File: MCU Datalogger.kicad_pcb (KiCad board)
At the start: 2 copper layers, 51.4 x 34.3 mm, 31 parts, among them J1 Conn_01x04_Male, J2 Conn_01x09_Male, J3 Conn_01x04_Male, J4 Conn_02x03_Odd_Even, U1 24LC1025, U2 DS1337S+, U3 24LC1025, U4 ATMEGA328P-AU, Y1 32.768 KHz, Y2 16 MHz

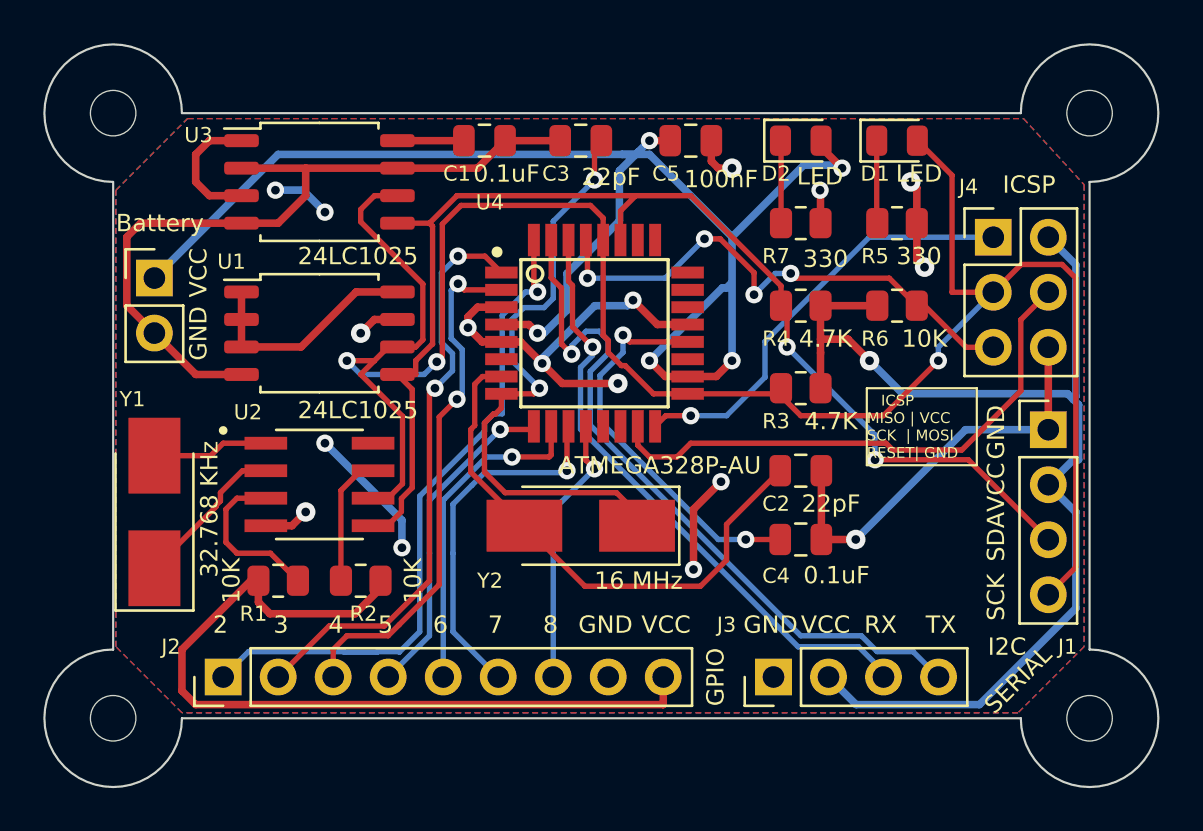
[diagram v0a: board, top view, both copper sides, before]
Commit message: Completed 4-layer pcb routing.
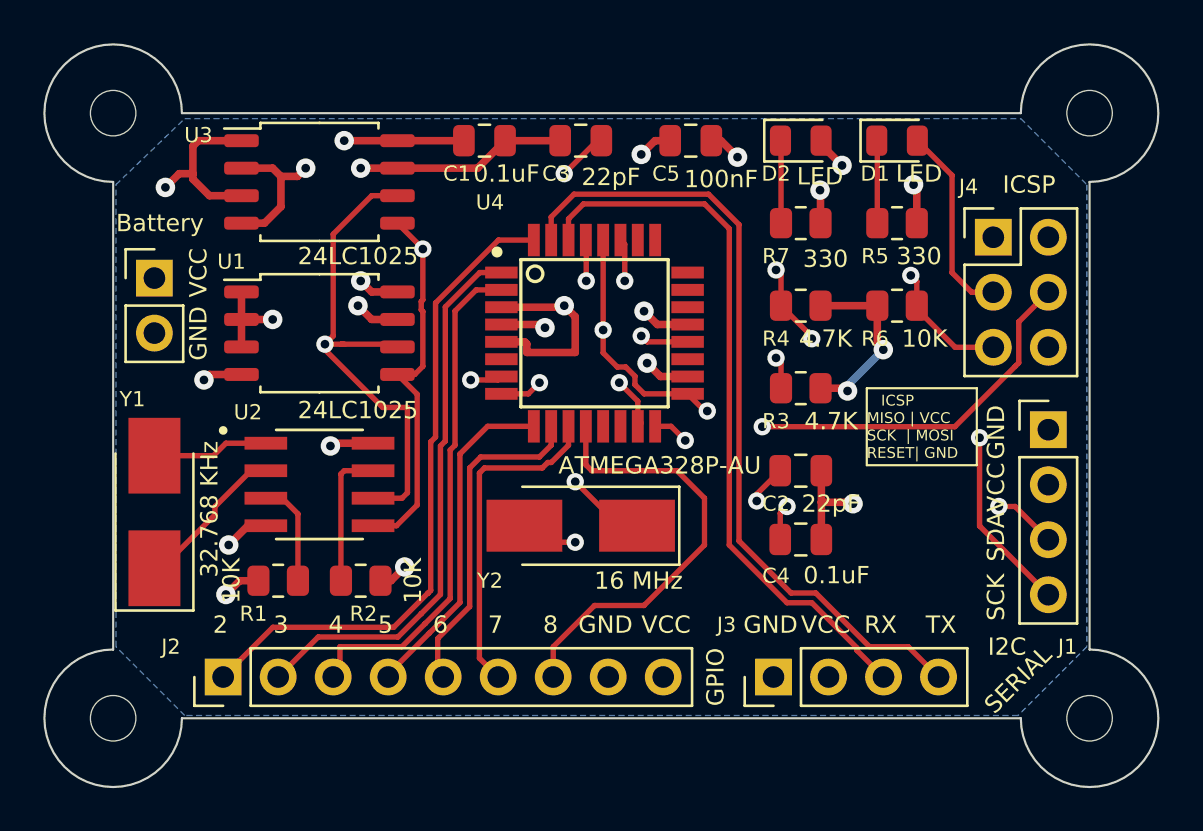
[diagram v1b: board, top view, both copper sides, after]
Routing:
- net /Vcc: track 188.4 -> 45.9 mm, vias 10 -> 13
- net GND: track 90.4 -> 43.5 mm, vias 13 -> 11
- net /D8: track 12.5 -> 20.4 mm, vias 1 -> 0
- net /SCK: track 98.0 -> 90.8 mm, vias 3 -> 5
- net /RX: track 28.3 -> 33.5 mm, vias 1 -> 0
- net Net-(Y2-Pad1): track 28.8 -> 24.8 mm, vias 2 -> 3
- net /TX: track 33.3 -> 37.2 mm, vias 1 -> 0
- net Net-(U2-Pad3): track 7.64 -> 4.87 mm
- net /SDA: track 58.3 -> 56.4 mm, vias 2 -> 5
- net /D7: track 16.9 -> 15.3 mm, vias 1 -> 0
- net /D3: track 27.2 -> 25.7 mm, vias 2 -> 0
- net /MOSI: track 25.4 -> 26.9 mm, vias 0 -> 2
- net /RESET: track 24.8 -> 23.7 mm, vias 4 -> 2
- net Net-(U4-Pad20): track 18.1 -> 18.9 mm
- net /D4: track 24.2 -> 23.5 mm, vias 2 -> 0
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- added copper zone on In2.Cu, net /Vcc
- removed copper zone on F.Cu, net /Vcc
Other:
- copper layers 2 -> 4

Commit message: Added board characteristics.
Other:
- board text added: "4.6900 mm"
- board text removed: "1.6000 mm"
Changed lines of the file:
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@@
       (plotinvisibletext false)
       (sketchpadsonfab false)
-      (subtractmaskfromsilk false)
+      (subtractmaskfromsilk true)
       (outputformat 1)
       (mirror false)
       (drillshape 0)
       (scaleselection 1)
-      (outputdirectory "MCU_Datalogger_Gerbers/")
+      (outputdirectory "4_layer_MCU_Datalogger_Gerbers")
     )
   )
@@
     (effects (font (size 0.8 0.8) (thickness 0.15)))
   )
-  (gr_text "Castellated pads: " (at 144.641 99.287) (layer "User.1")
+  (gr_text "Min track/spacing: " (at 146.8 90.13) (layer "User.1")
     (effects (font (size 1.5 1.5) (thickness 0.2)) (justify left top))
   )
-  (gr_text "No" (at 236.098143 99.287) (layer "User.1")
+  (gr_text "4.6900 mm" (at 238.257143 81.1) (layer "User.1")
     (effects (font (size 1.5 1.5) (thickness 0.2)) (justify left top))
   )
-  (gr_text "None" (at 177.198143 94.772) (layer "User.1")
+  (gr_text "Impedance Control: " (at 213.414286 94.645) (layer "User.1")
     (effects (font (size 1.5 1.5) (thickness 0.2)) (justify left top))
   )
-  (gr_text "1.6000 mm" (at 236.098143 81.227) (layer "User.1")
+  (gr_text "Board overall dimensions: " (at 146.8 85.615) (layer "User.1")
     (effects (font (size 1.5 1.5) (thickness 0.2)) (justify left top))
   )
-  (gr_text "" (at 211.255286 85.742) (layer "User.1")
+  (gr_text "0.2000 mm / 0.0000 mm" (at 179.357143 90.13) (layer "User.1")
     (effects (font (size 1.5 1.5) (thickness 0.2)) (justify left top))
   )
-  (gr_text "51.7350 mm x 34.5900 mm" (at 177.198143 85.742) (layer "User.1")
+  (gr_text "" (at 238.257143 85.615) (layer "User.1")
     (effects (font (size 1.5 1.5) (thickness 0.2)) (justify left top))
   )
-  (gr_text "0.2000 mm / 0.0000 mm" (at 177.198143 90.257) (layer "User.1")
+  (gr_text "51.7350 mm x 34.5900 mm" (at 179.357143 85.615) (layer "User.1")
     (effects (font (size 1.5 1.5) (thickness 0.2)) (justify left top))
   )
-  (gr_text "Min track/spacing: " (at 144.641 90.257) (layer "User.1")
+  (gr_text "Copper Layer Count: " (at 146.8 81.1) (layer "User.1")
     (effects (font (size 1.5 1.5) (thickness 0.2)) (justify left top))
   )
-  (gr_text "Min hole diameter: " (at 211.255286 90.257) (layer "User.1")
+  (gr_text "4" (at 179.357143 81.1) (layer "User.1")
     (effects (font (size 1.5 1.5) (thickness 0.2)) (justify left top))
   )
-  (gr_text "Board overall dimensions: " (at 144.641 85.742) (layer "User.1")
+  (gr_text "No" (at 238.257143 99.16) (layer "User.1")
     (effects (font (size 1.5 1.5) (thickness 0.2)) (justify left top))
   )
-  (gr_text "0.3000 mm" (at 236.098143 90.257) (layer "User.1")
+  (gr_text "Castellated pads: " (at 146.8 99.16) (layer "User.1")
     (effects (font (size 1.5 1.5) (thickness 0.2)) (justify left top))
   )
-  (gr_text "2" (at 177.198143 81.227) (layer "User.1")
+  (gr_text "Copper Finish: " (at 146.8 94.645) (layer "User.1")
     (effects (font (size 1.5 1.5) (thickness 0.2)) (justify left top))
   )
-  (gr_text "" (at 236.098143 85.742) (layer "User.1")
+  (gr_text "" (at 213.414286 85.615) (layer "User.1")
     (effects (font (size 1.5 1.5) (thickness 0.2)) (justify left top))
   )
-  (gr_text "Board Thickness: " (at 211.255286 81.227) (layer "User.1")
+  (gr_text "None" (at 179.357143 94.645) (layer "User.1")
     (effects (font (size 1.5 1.5) (thickness 0.2)) (justify left top))
   )
-  (gr_text "No" (at 236.098143 94.772) (layer "User.1")
+  (gr_text "Board Thickness: " (at 213.414286 81.1) (layer "User.1")
     (effects (font (size 1.5 1.5) (thickness 0.2)) (justify left top))
   )
-  (gr_text "Copper Layer Count: " (at 144.641 81.227) (layer "User.1")
+  (gr_text "No" (at 179.357143 99.16) (layer "User.1")
     (effects (font (size 1.5 1.5) (thickness 0.2)) (justify left top))
   )
-  (gr_text "Plated Board Edge: " (at 211.255286 99.287) (layer "User.1")
+  (gr_text "Min hole diameter: " (at 213.414286 90.13) (layer "User.1")
     (effects (font (size 1.5 1.5) (thickness 0.2)) (justify left top))
   )
-  (gr_text "BOARD CHARACTERISTICS" (at 143.891 75.057) (layer "User.1")
-    (effects (font (size 2 2) (thickness 0.4)) (justify left top))
-  )
-  (gr_text "Impedance Control: " (at 211.255286 94.772) (layer "User.1")
+  (gr_text "Plated Board Edge: " (at 213.414286 99.16) (layer "User.1")
     (effects (font (size 1.5 1.5) (thickness 0.2)) (justify left top))
   )
-  (gr_text "No" (at 177.198143 99.287) (layer "User.1")
+  (gr_text "0.3000 mm" (at 238.257143 90.13) (layer "User.1")
     (effects (font (size 1.5 1.5) (thickness 0.2)) (justify left top))
   )
-  (gr_text "Copper Finish: " (at 144.641 94.772) (layer "User.1")
+  (gr_text "No" (at 238.257143 94.645) (layer "User.1")
     (effects (font (size 1.5 1.5) (thickness 0.2)) (justify left top))
   )
+  (gr_text "BOARD CHARACTERISTICS" (at 146.05 74.93) (layer "User.1")
+    (effects (font (size 2 2) (thickness 0.4)) (justify left top))
+  )
   (segment (start 126.172 92.898) (end 126.238 92.964) (width 0.35) (layer "F.Cu") (net 1))
   (segment (start 124.775 92.898) (end 124.775 94.615) (width 0.35) (layer "F.Cu") (net 1))
@@
     )
   )
-  (group "group-boardCharacteristics" (id 5543f652-5764-4088-ab8c-8fbb9285404a)
+  (group "group-boardCharacteristics" (id 094f15a9-67f1-4bb2-8cee-223c176f5df0)
     (members
-      28a1d238-59f6-4a35-a5dc-af4c1141d087
-      2e46d89e-0d48-4348-85a3-df1ce8749473
-      3337a5c1-46a8-44b2-ae17-85742c382bbc
-      3e00147c-7f39-4c86-be06-0bc88671f63a
-      44829b3a-1615-418a-95a6-4fa380619e0c
-      552e15e3-a909-4e5f-b0c2-e4e84c63fd2e
-      60b29d79-869e-4ace-8478-7d224f92b1a8
-      6860e647-974f-4d4e-a5d1-57925d9c9715
-      7f9653d2-7263-4b83-9102-d0f350d89f51
-      7fdd53a2-efb2-416b-b70e-3b5deac404b5
-      82a7bc8e-4ec0-4b1d-8242-e3b35b4fb704
-      a346d7ef-a499-40f2-b098-aad555c6fb95
-      a6a6436b-05e8-4fe1-88a6-66219fefb188
-      ce06e2ef-deab-42df-873a-182126005c86
-      d5e81698-0c91-4435-af86-53d265a30b3b
-      def9a921-cc64-4743-a27a-1b37b301737d
-      e5aff48d-d5b1-436f-94d9-7b16cc2fe21d
-      e6945b51-5ce6-472c-a97a-b11645a4e915
-      f2fa58d2-1612-4a13-adf6-4fa57ed7e63c
-      fa12292c-2a74-432f-a29b-336ebc171599
-      fe83dda4-587e-4723-be3a-9b959bdd26c1
+      14790a37-0d0e-422f-88a8-0f0ad7192f32
+      1bfcf1ed-c21d-4eae-9501-8c2714b8c4fd
+      35e8a65f-fe75-462f-af9b-d5ba8c7b4807
+      3ad38b3f-730d-44e3-bc85-8b0d371a8f13
+      50298d8a-4e10-4eee-a0a0-1bfce37cc08c
+      54995e15-a228-4c10-90ee-dbb4d79569df
+      5739516b-e12a-4d6b-8778-423ebaa58d12
+      76949556-130a-4a6b-a132-23f6ac437df0
+      7b24b4bc-eaf2-44fe-8896-5cb385609016
+      7cd46077-870a-4086-b819-efc14b4d7de1
+      7e158de1-3eac-4843-ab83-be77d4b53599
+      8d3d3363-7f98-400e-a3e5-15f49f0c7917
+      9e782aba-076c-414e-97ae-de8698fbe63c
+      d97f9bc7-24d4-498b-943b-b1128c8eaaea
+      e25ae54a-c407-479b-963c-8f8fce2872f0
+      eabfe026-196f-4eb8-a6b6-f570294beeb2
+      ecd44d22-18fc-4369-9b7c-2e8fb255ef96
+      f0953841-db38-450e-999f-7dc596792a6d
+      f42c304c-9c5f-4388-97b5-e8ad03f9c648
+      f612a90d-2a8e-436d-9bd7-b03a328324a3
+      fc6e8742-6bd7-45b3-907f-0cc7ad67140b
     )
   )

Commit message: Imported changes from schematic.
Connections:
- net Net-(U4-Pad20) renamed /Abc123
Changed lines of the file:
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@@
   (net 1 "GND")
   (net 2 "/Vcc")
-  (net 3 "Net-(Y2-Pad2)")
-  (net 4 "Net-(Y2-Pad1)")
-  (net 5 "Net-(U4-Pad20)")
-  (net 6 "Net-(R5-Pad2)")
+  (net 3 "Net-(C2-Pad2)")
+  (net 4 "Net-(C3-Pad2)")
+  (net 5 "/Abc123")
+  (net 6 "Net-(D1-Pad1)")
   (net 7 "/SCK")
-  (net 8 "Net-(R7-Pad1)")
+  (net 8 "Net-(D2-Pad1)")
   (net 9 "/SDA")
   (net 10 "/D2")
@@
   (net 20 "/MOSI")
   (net 21 "/RESET")
-  (net 22 "Net-(U2-Pad3)")
+  (net 22 "Net-(R1-Pad2)")
   (net 23 "Net-(R2-Pad2)")
   (net 24 "Net-(U2-Pad1)")
-  (net 25 "Net-(Y1-Pad1)")
+  (net 25 "Net-(U2-Pad2)")
   (footprint "MountingHole:MountingHole_2.1mm" (layer "F.Cu")
     (at 137.16 102.87)
@@
       (net 2 "/Vcc") (pintype "passive"))
     (pad "2" smd roundrect locked (at 0.9125 0) (size 1.025 1.4) (layers "F.Cu" "F.Paste" "F.Mask") (roundrect_rratio 0.243902439)
-      (net 22 "Net-(U2-Pad3)") (pintype "passive"))
+      (net 22 "Net-(R1-Pad2)") (pintype "passive"))
     (model "${KICAD6_3DMODEL_DIR}/Resistor_SMD.3dshapes/R_0805_2012Metric.wrl"
       (offset (xyz 0 0 0))
@@
       (net 1 "GND") (pintype "passive"))
     (pad "2" smd roundrect locked (at 0.95 0 180) (size 1 1.45) (layers "F.Cu" "F.Paste" "F.Mask") (roundrect_rratio 0.25)
-      (net 3 "Net-(Y2-Pad2)") (pintype "passive"))
+      (net 3 "Net-(C2-Pad2)") (pintype "passive"))
     (model "${KICAD6_3DMODEL_DIR}/Capacitor_SMD.3dshapes/C_0805_2012Metric.wrl"
       (offset (xyz 0 0 0))
@@
     (fp_line (start -1 0.625) (end -1 -0.625) (layer "F.Fab") (width 0.1))
     (pad "1" smd roundrect locked (at -0.9125 0) (size 1.025 1.4) (layers "F.Cu" "F.Paste" "F.Mask") (roundrect_rratio 0.243902439)
-      (net 2 "/Vcc"))
+      (net 2 "/Vcc") (pintype "passive"))
     (pad "2" smd roundrect locked (at 0.9125 0) (size 1.025 1.4) (layers "F.Cu" "F.Paste" "F.Mask") (roundrect_rratio 0.243902439)
-      (net 21 "/RESET"))
+      (net 21 "/RESET") (pintype "passive"))
     (model "${KICAD6_3DMODEL_DIR}/Resistor_SMD.3dshapes/R_0805_2012Metric.wrl"
       (offset (xyz 0 0 0))
@@
     (fp_line (start -0.7 -0.6) (end -1 -0.3) (layer "F.Fab") (width 0.1))
     (pad "1" smd roundrect locked (at -0.9375 0) (size 0.975 1.4) (layers "F.Cu" "F.Paste" "F.Mask") (roundrect_rratio 0.25)
-      (net 6 "Net-(R5-Pad2)") (pinfunction "K") (pintype "passive"))
+      (net 6 "Net-(D1-Pad1)") (pinfunction "K") (pintype "passive"))
     (pad "2" smd roundrect locked (at 0.9375 0) (size 0.975 1.4) (layers "F.Cu" "F.Paste" "F.Mask") (roundrect_rratio 0.25)
       (net 7 "/SCK") (pinfunction "A") (pintype "passive"))
@@
     (fp_line (start 1 -0.625) (end 1 0.625) (layer "F.Fab") (width 0.1))
     (pad "1" smd roundrect locked (at -0.9125 0) (size 1.025 1.4) (layers "F.Cu" "F.Paste" "F.Mask") (roundrect_rratio 0.243902439)
-      (net 8 "Net-(R7-Pad1)") (pintype "passive"))
+      (net 8 "Net-(D2-Pad1)") (pintype "passive"))
     (pad "2" smd roundrect locked (at 0.9125 0) (size 1.025 1.4) (layers "F.Cu" "F.Paste" "F.Mask") (roundrect_rratio 0.243902439)
       (net 1 "GND") (pintype "passive"))
@@
       (net 1 "GND") (pintype "passive"))
     (pad "2" smd roundrect locked (at 0.9125 0 180) (size 1.025 1.4) (layers "F.Cu" "F.Paste" "F.Mask") (roundrect_rratio 0.243902439)
-      (net 6 "Net-(R5-Pad2)") (pintype "passive"))
+      (net 6 "Net-(D1-Pad1)") (pintype "passive"))
     (model "${KICAD6_3DMODEL_DIR}/Resistor_SMD.3dshapes/R_0805_2012Metric.wrl"
       (offset (xyz 0 0 0))
@@
     (fp_line (start -2.3 -1.6) (end 2.3 -1.6) (layer "F.Fab") (width 0.1))
     (pad "1" smd rect locked (at -2.6 0 180) (size 3.5 2.4) (layers "F.Cu" "F.Paste" "F.Mask")
-      (net 4 "Net-(Y2-Pad1)") (pinfunction "1") (pintype "passive"))
+      (net 4 "Net-(C3-Pad2)") (pinfunction "1") (pintype "passive"))
     (pad "2" smd rect locked (at 2.6 0 180) (size 3.5 2.4) (layers "F.Cu" "F.Paste" "F.Mask")
-      (net 3 "Net-(Y2-Pad2)") (pinfunction "2") (pintype "passive"))
+      (net 3 "Net-(C2-Pad2)") (pinfunction "2") (pintype "passive"))
     (model "${KICAD6_3DMODEL_DIR}/Crystal.3dshapes/Crystal_SMD_0603-2Pin_6.0x3.5mm.step"
       (offset (xyz 0 0 0))
@@
       (net 1 "GND") (pintype "passive"))
     (pad "2" smd roundrect locked (at 0.95 0 180) (size 1 1.45) (layers "F.Cu" "F.Paste" "F.Mask") (roundrect_rratio 0.25)
-      (net 5 "Net-(U4-Pad20)") (pintype "passive"))
+      (net 5 "/Abc123") (pintype "passive"))
     (model "${KICAD6_3DMODEL_DIR}/Capacitor_SMD.3dshapes/C_0805_2012Metric.wrl"
       (offset (xyz 0 0 0))
@@
     (fp_line (start 1 -0.6) (end -0.7 -0.6) (layer "F.Fab") (width 0.1))
     (pad "1" smd roundrect locked (at -0.9375 0) (size 0.975 1.4) (layers "F.Cu" "F.Paste" "F.Mask") (roundrect_rratio 0.25)
-      (net 8 "Net-(R7-Pad1)") (pinfunction "K") (pintype "passive"))
+      (net 8 "Net-(D2-Pad1)") (pinfunction "K") (pintype "passive"))
     (pad "2" smd roundrect locked (at 0.9375 0) (size 0.975 1.4) (layers "F.Cu" "F.Paste" "F.Mask") (roundrect_rratio 0.25)
       (net 2 "/Vcc") (pinfunction "A") (pintype "passive"))
@@
       (net 1 "GND") (pintype "passive"))
     (pad "2" smd roundrect locked (at 0.95 0) (size 1 1.45) (layers "F.Cu" "F.Paste" "F.Mask") (roundrect_rratio 0.25)
-      (net 4 "Net-(Y2-Pad1)") (pintype "passive"))
+      (net 4 "Net-(C3-Pad2)") (pintype "passive"))
     (model "${KICAD6_3DMODEL_DIR}/Capacitor_SMD.3dshapes/C_0805_2012Metric.wrl"
       (offset (xyz 0 0 0))
@@
       (pinfunction "VCC") (pintype "power_in+no_connect"))
     (pad "7" smd rect locked (at -4.3 2) (size 1.5 0.55) (layers "F.Cu" "F.Paste" "F.Mask")
-      (net 3 "Net-(Y2-Pad2)") (pinfunction "PB6") (pintype "bidirectional"))
+      (net 3 "Net-(C2-Pad2)") (pinfunction "PB6") (pintype "bidirectional"))
     (pad "8" smd rect locked (at -4.3 2.8) (size 1.5 0.55) (layers "F.Cu" "F.Paste" "F.Mask")
-      (net 4 "Net-(Y2-Pad1)") (pinfunction "PB7") (pintype "bidirectional"))
+      (net 4 "Net-(C3-Pad2)") (pinfunction "PB7") (pintype "bidirectional"))
     (pad "9" smd rect locked (at -2.8 4.3) (size 0.55 1.5) (layers "F.Cu" "F.Paste" "F.Mask")
       (net 13 "/D5") (pinfunction "PD5") (pintype "bidirectional"))
@@
       (pinfunction "ADC6") (pintype "bidirectional+no_connect"))
     (pad "20" smd rect locked (at 4.3 0.4) (size 1.5 0.55) (layers "F.Cu" "F.Paste" "F.Mask")
-      (net 5 "Net-(U4-Pad20)") (pinfunction "AREF") (pintype "input"))
+      (net 5 "/Abc123") (pinfunction "AREF") (pintype "input"))
     (pad "21" smd rect locked (at 4.3 -0.4) (size 1.5 0.55) (layers "F.Cu" "F.Paste" "F.Mask")
       (net 1 "GND") (pinfunction "GND") (pintype "power_in"))
@@
       (net 24 "Net-(U2-Pad1)") (pinfunction "X1") (pintype "input"))
     (pad "2" smd rect locked (at -2.475 -0.635) (size 1.97 0.59) (layers "F.Cu" "F.Paste" "F.Mask")
-      (net 25 "Net-(Y1-Pad1)") (pinfunction "X2") (pintype "bidirectional"))
+      (net 25 "Net-(U2-Pad2)") (pinfunction "X2") (pintype "bidirectional"))
     (pad "3" smd rect locked (at -2.475 0.635) (size 1.97 0.59) (layers "F.Cu" "F.Paste" "F.Mask")
-      (net 22 "Net-(U2-Pad3)") (pinfunction "~INTA") (pintype "output"))
+      (net 22 "Net-(R1-Pad2)") (pinfunction "~INTA") (pintype "output"))
     (pad "4" smd rect locked (at -2.475 1.905) (size 1.97 0.59) (layers "F.Cu" "F.Paste" "F.Mask")
       (net 1 "GND") (pinfunction "GND") (pintype "power_in"))
@@
     (fp_line (start -2.3 1.6) (end -2.5 1.4) (layer "F.Fab") (width 0.1))
     (pad "1" smd rect locked (at -2.6 0 90) (size 3.5 2.4) (layers "F.Cu" "F.Paste" "F.Mask")
-      (net 25 "Net-(Y1-Pad1)") (pinfunction "1") (pintype "passive"))
+      (net 25 "Net-(U2-Pad2)") (pinfunction "1") (pintype "passive"))
     (pad "2" smd rect locked (at 2.6 0 90) (size 3.5 2.4) (layers "F.Cu" "F.Paste" "F.Mask")
       (net 24 "Net-(U2-Pad1)") (pinfunction "2") (pintype "passive"))
